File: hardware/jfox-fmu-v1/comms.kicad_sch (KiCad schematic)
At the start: 6 parts, among them J30 USB-C, J31 microSD, U30 ISOW1044, U31 ISOW1044

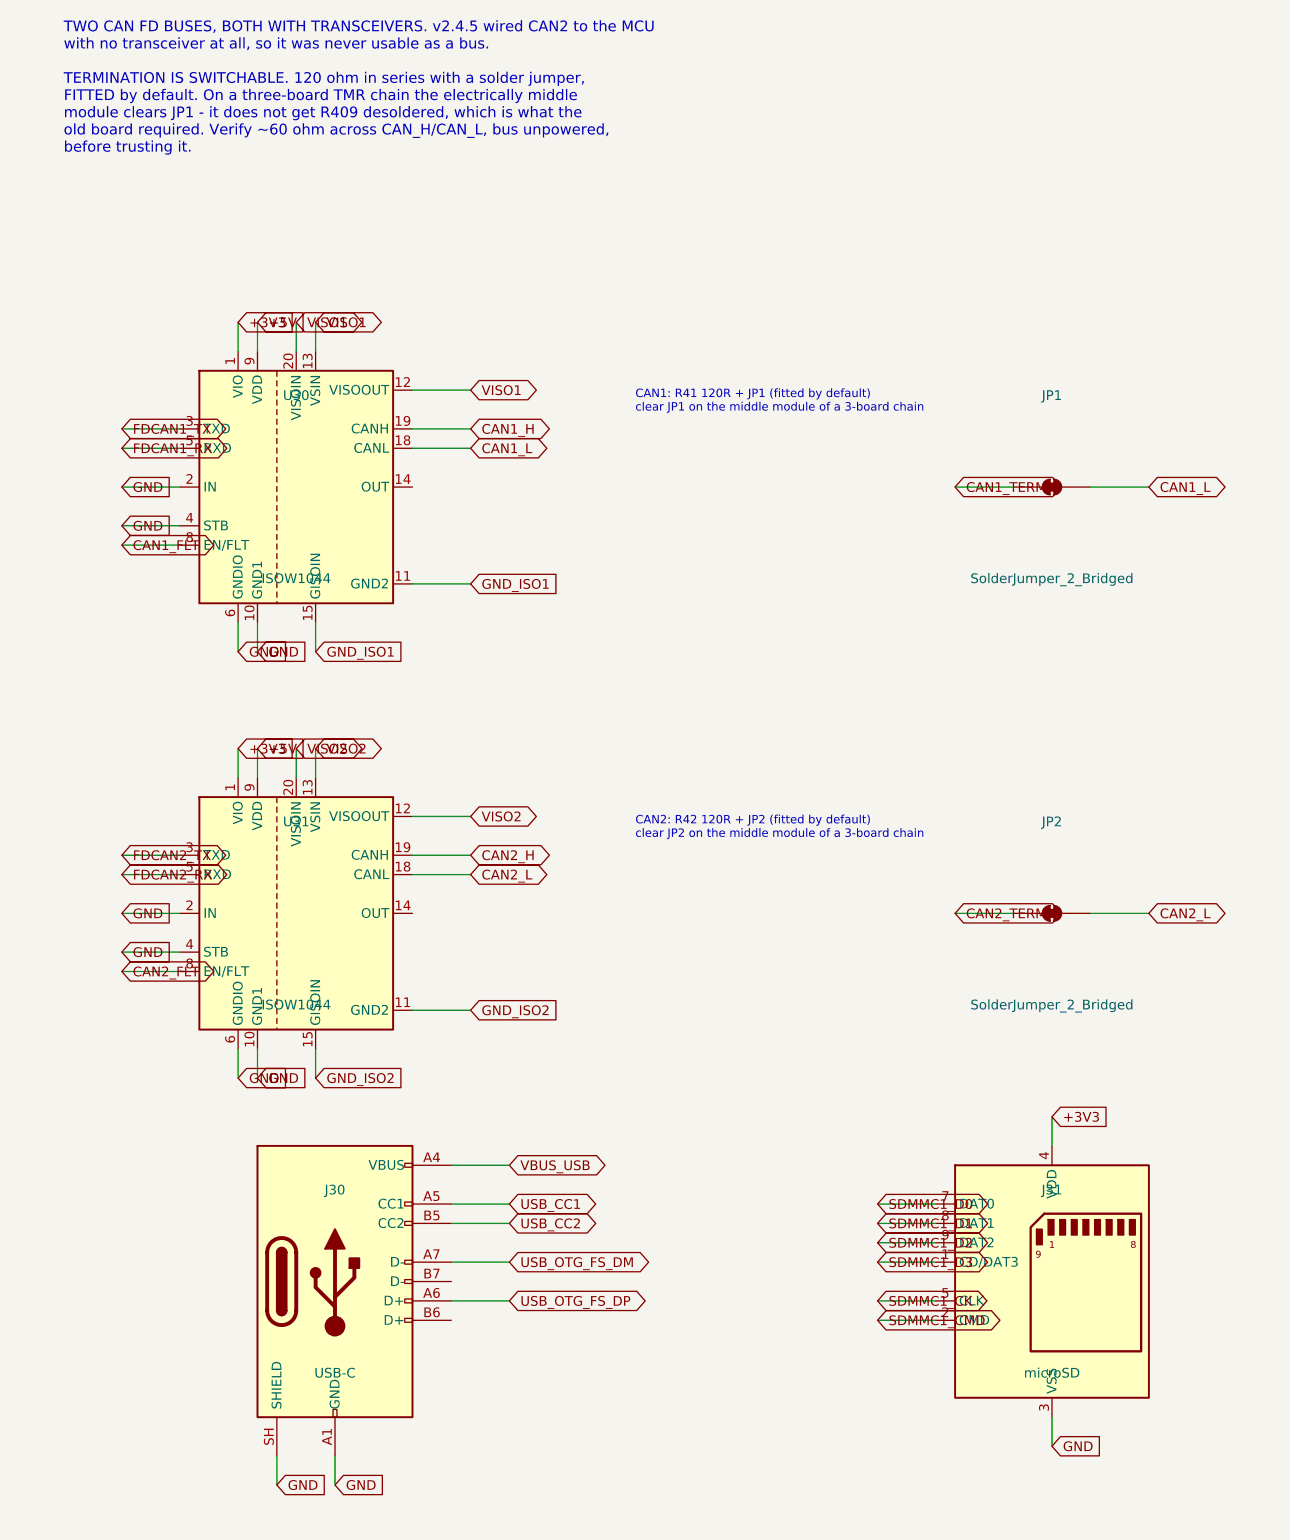
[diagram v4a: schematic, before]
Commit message: microSD with card detect, and the storage split made explicit
The socket was already on the board and every SDMMC line was wired, but it
used Connector:SD_Card_Device - a symbol with no card-detect pin and no
shield. SD_DETECT therefore had an MCU pin allocated and no source, and the
shield floated.

Swapped to Connector:Micro_SD_Card_Det_Hirose_DM3AT, which is the same socket
the footprint was already chosen for and exposes the DET_A/DET_B mechanical
switch plus SHIELD. DET_B grounds, DET_A is pulled up and read, so firmware
can tell "no card" from "card present but failing". Those need different
responses - the first is a pre-flight nag, the second is a logging fault - and
without card detect they are indistinguishable.

Six pull-ups added. The SD specification requires CMD and DAT0-3 held high,
and DAT3 doubles as the card's own detect pin so it must not float during
initialisation. The STM32's internal pull-ups exist but are weak and only
come up after GPIO configuration, which is after the card has already sampled
the bus.

Isolated nets: 1 -> 0. Every net on this board now reaches at least two pins.

On what the card is FOR, since the request was about parameters: it is not
where parameters go, and it should not be.

Parameters and calibration stay in the FM25V02A FRAM, which is where
flight::calibration::storage already writes them - with a "JFOX" magic word
and an FNV-1a checksum so a blank or corrupted record can never read as
valid. FRAM has unlimited write endurance, needs no filesystem, and cannot be
corrupted by power loss mid-write. An SD card can be pulled out, wears out,
and corrupts on power loss during a block write. Putting calibration there
would be a downgrade dressed as convenience.

The card is for flight logs: large, sequential, expendable - the opposite of
parameters, and exactly what the medium is good at. HWR-IFC-006 now says
FRAM explicitly rather than "non-volatile storage", and HWR-IFC-007 covers
the socket, so the distinction is record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
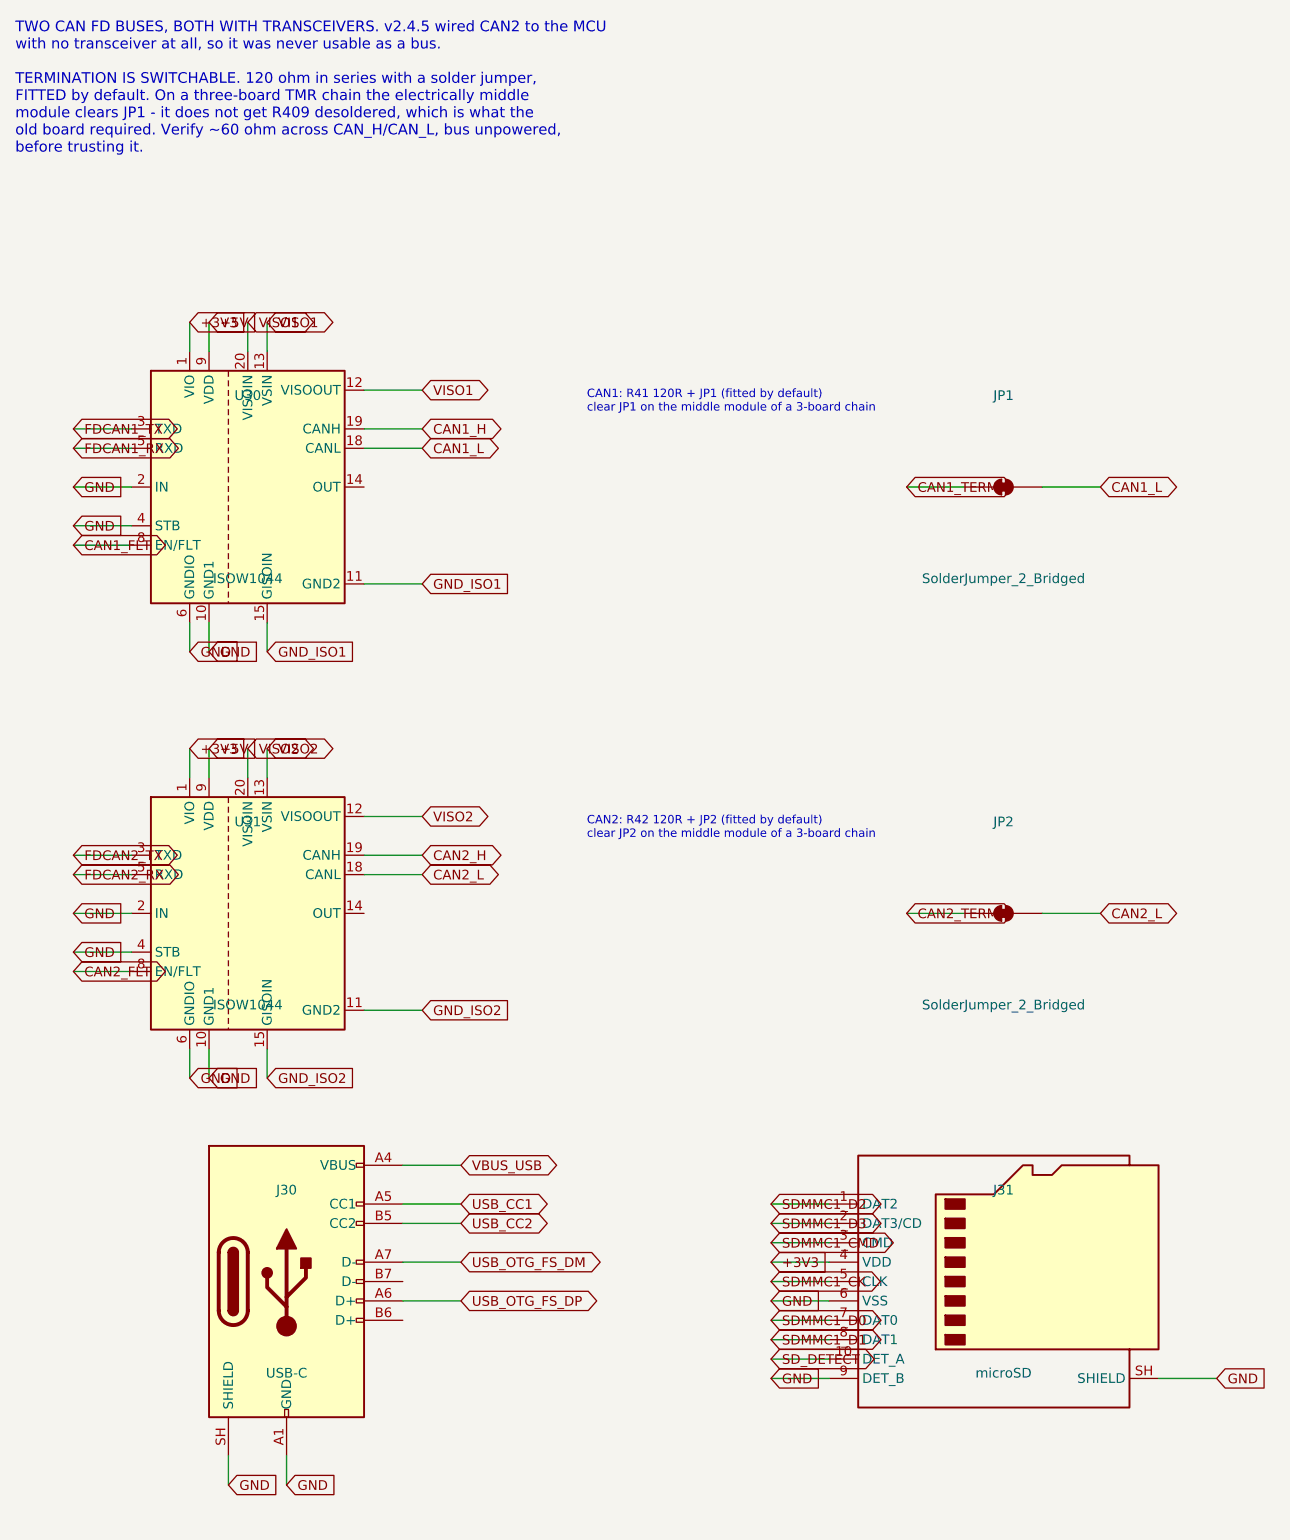
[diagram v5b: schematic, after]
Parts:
- removed J31: microSD, Connector_Card:microSD_HC_Hirose_DM3AT-SF-PEJM5, symbol Connector:SD_Card_Device
- added J31: microSD, Connector_Card:microSD_HC_Hirose_DM3AT-SF-PEJM5, symbol Connector:Micro_SD_Card_Det_Hirose_DM3AT
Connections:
- net +3V3: now also J31.4 (VDD)
- net GND: now also J31.6 (VSS), J31.9 (DET_B), J31.SH (SHIELD)
- net SDMMC1_CK: now also J31.5 (CLK)
- net SDMMC1_CMD: now also J31.3 (CMD)
- net SDMMC1_D0: now also J31.7 (DAT0)
- net SDMMC1_D1: now also J31.8 (DAT1)
- net SDMMC1_D2: now also J31.1 (DAT2)
- net SDMMC1_D3: now also J31.2 (DAT3/CD)
- new net SD_DETECT: J31.10 (DET_A)

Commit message: EMI/EMC protection, and the stackup that actually decides it
Full review first: schematic, footprints, sheet fit and traceability all pass;
objective passes 12 of 13 with fibre the only gap; environmental passes the
category and reports its known gaps. ERC 89, of which 75 are deliberately
unallocated GPIO.

A new protection sheet closes HWR-ENV-006 and HWR-ENV-007, and adds the
emissions control that DO-160G s21 would otherwise fail on. This board carries
two deliberate switching sources - U21 at 2.5 MHz and each ISOW1044's internal
converter at 25 MHz - and every off-board harness is an antenna bonded to
them.

  D4/D5/D6  6 V TVS on brick, servo and USB inputs. Above the 5.5 V a valid
            supply reaches, below what the LTC4417 and the buck tolerate.
            Unidirectional - reverse battery is the LTC4417's job.
  U40       USBLC6-2SC6 between J30 and the choke, closest to the connector
            so it protects the choke too, not only the MCU.
  L5        common-mode choke on USB, after the ESD array.
  L3/L4     common-mode chokes on both CAN pairs, with D7/D8 across them.
  FB1-3     ferrites on the 5 V feed to the telemetry, GPS and RC harnesses,
            because conducted emissions leave on the power wire as readily as
            on the signal wires.

The CAN protection references GND_ISO, not GND. Referencing it to board ground
would bridge the isolation barrier and undo the reason the ISOW1044 is there.

PCB_STACKUP_AND_EMC.md carries the half of EMC that is not a component:

**Six layers, not four.** A 4-layer SIG/GND/PWR/SIG leaves the inner power
layer split - and this board splits it four ways for the switched sensor rails
plus the analog and isolated domains. A signal crossing a split has no return
beneath it, so the return detours and the loop it encloses is the radiating
element. Six layers puts solid ground either side of the power layer, so every
signal has an unbroken return whatever the power layer is doing. That is the
single mos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
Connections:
- net USB_OTG_FS_DM renamed USB_DM_RAW
- net USB_OTG_FS_DP renamed USB_DP_RAW
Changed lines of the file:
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@@
 		(instances
 			(project "jfox-fmu"
-				(path "/ed69d7f7-ecc0-4770-a099-fc7c46f3e48b"
+				(path "/cad398bc-936f-4ddc-9b54-c34d64f6ea2c"
 					(reference "U30")
 					(unit 1)
@@
 		(instances
 			(project "jfox-fmu"
-				(path "/ed69d7f7-ecc0-4770-a099-fc7c46f3e48b"
+				(path "/cad398bc-936f-4ddc-9b54-c34d64f6ea2c"
 					(reference "JP1")
 					(unit 1)
@@
 		(instances
 			(project "jfox-fmu"
-				(path "/ed69d7f7-ecc0-4770-a099-fc7c46f3e48b"
+				(path "/cad398bc-936f-4ddc-9b54-c34d64f6ea2c"
 					(reference "U31")
 					(unit 1)
@@
 		(instances
 			(project "jfox-fmu"
-				(path "/ed69d7f7-ecc0-4770-a099-fc7c46f3e48b"
+				(path "/cad398bc-936f-4ddc-9b54-c34d64f6ea2c"
 					(reference "JP2")
 					(unit 1)
@@
 		(instances
 			(project "jfox-fmu"
-				(path "/ed69d7f7-ecc0-4770-a099-fc7c46f3e48b"
+				(path "/cad398bc-936f-4ddc-9b54-c34d64f6ea2c"
 					(reference "J30")
 					(unit 1)
@@
 		)
 	)
-	(global_label "USB_OTG_FS_DP"
+	(global_label "USB_DP_RAW"
 		(shape bidirectional)
 		(at 83.82 181.61 180)
@@
 		)
 	)
-	(global_label "USB_OTG_FS_DM"
+	(global_label "USB_DM_RAW"
 		(shape bidirectional)
 		(at 83.82 176.53 180)
@@
 		(instances
 			(project "jfox-fmu"
-				(path "/ed69d7f7-ecc0-4770-a099-fc7c46f3e48b"
+				(path "/cad398bc-936f-4ddc-9b54-c34d64f6ea2c"
 					(reference "J31")
 					(unit 1)
